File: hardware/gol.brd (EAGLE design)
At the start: 67.3 x 67.3 mm, 70 parts, among them J1 TC2050-IDC, J2 2057-MCR-B-S-RA-TSMT-NP-CS4-T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, U1 STM32F072CBT, U2 AP2111H-3.3TRG1SOT-223_DIO-M

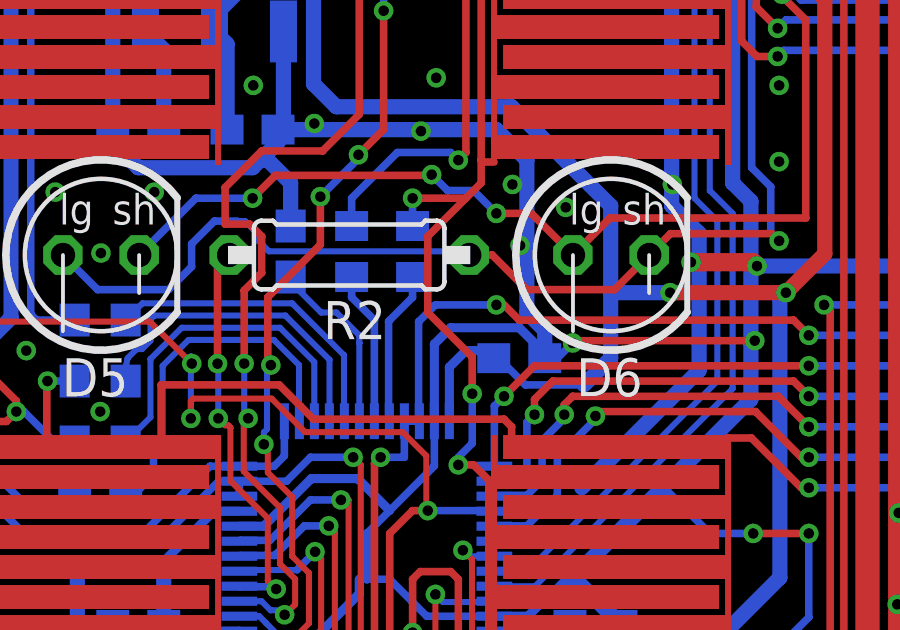
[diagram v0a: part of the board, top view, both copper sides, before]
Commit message: fills in an orphan
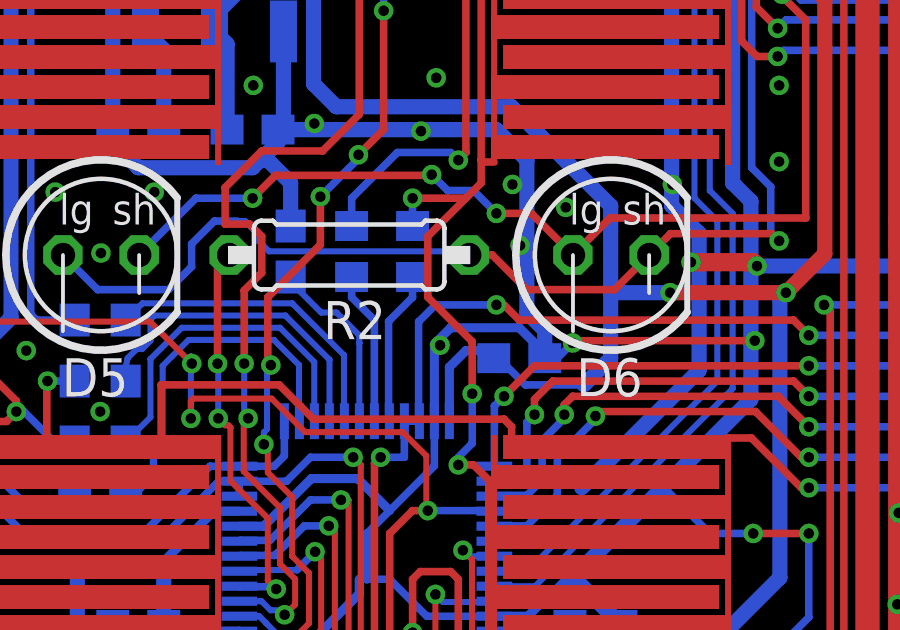
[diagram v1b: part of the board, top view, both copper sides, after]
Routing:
- net GND: vias 164 -> 165
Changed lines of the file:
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@@
 <via x="20.3708" y="11.0998" extent="1-16" drill="0.35"/>
 <via x="23.749" y="9.8806" extent="1-16" drill="0.35"/>
+<via x="24.0284" y="35.9918" extent="1-16" drill="0.35"/>
 </signal>
 <signal name="CAN_TR">
@@
 <wire x1="25.100803125" y1="32.720803125" x2="25.100803125" y2="34.377003125" width="0.254" layer="16"/>
 <via x="25.100803125" y="34.377003125" extent="1-16" drill="0.35"/>
-<wire x1="25.100803125" y1="34.377003125" x2="25.100803125" y2="35.605196875" width="0.254" layer="1"/>
-<wire x1="23.622" y1="37.084" x2="23.622" y2="39.624" width="0.254" layer="1"/>
+<wire x1="25.100803125" y1="34.377003125" x2="25.100803125" y2="36.113196875" width="0.254" layer="1"/>
+<wire x1="23.622" y1="37.592" x2="23.622" y2="39.624" width="0.254" layer="1"/>
 <wire x1="23.622" y1="39.624" x2="24.892" y2="40.894" width="0.254" layer="1"/>
 <wire x1="24.638" y1="32.258" x2="25.100803125" y2="32.720803125" width="0.254" layer="16"/>
-<wire x1="25.100803125" y1="35.605196875" x2="23.622" y2="37.084" width="0.254" layer="1"/>
+<wire x1="25.100803125" y1="36.113196875" x2="23.622" y2="37.592" width="0.254" layer="1"/>
 <wire x1="25.83" y1="25.1" x2="26.416" y2="24.514" width="0.254" layer="1"/>
 <wire x1="26.416" y1="24.514" x2="26.416" y2="24.384" width="0.254" layer="1"/>

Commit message: adds right-angle female header. replaces north with this.
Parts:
- BTN17: value BOOT -> FLASH
- NORTH: device pinhead:1X04/90 -> parts:JP4-RA-FEM
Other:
- board text added: "(c) bracz 2023-06-23"
- board text added: "+5V"
- board text added: "G"
- board text added: "GLB"
- board text added: "GND"
- board text added: "L"
- board text added: "LOC"
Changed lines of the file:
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@@
 <layers>
 <layer number="1" name="Top" color="4" fill="1" visible="yes" active="yes"/>
-<layer number="16" name="Bottom" color="1" fill="1" visible="yes" active="yes"/>
+<layer number="16" name="Bottom" color="1" fill="1" visible="no" active="yes"/>
 <layer number="17" name="Pads" color="2" fill="1" visible="yes" active="yes"/>
 <layer number="18" name="Vias" color="2" fill="1" visible="yes" active="yes"/>
@@
 <layer number="20" name="Dimension" color="24" fill="1" visible="yes" active="yes"/>
 <layer number="21" name="tPlace" color="7" fill="1" visible="yes" active="yes"/>
-<layer number="22" name="bPlace" color="7" fill="1" visible="yes" active="yes"/>
+<layer number="22" name="bPlace" color="7" fill="1" visible="no" active="yes"/>
 <layer number="23" name="tOrigins" color="15" fill="1" visible="yes" active="yes"/>
-<layer number="24" name="bOrigins" color="15" fill="1" visible="yes" active="yes"/>
+<layer number="24" name="bOrigins" color="15" fill="1" visible="no" active="yes"/>
 <layer number="25" name="tNames" color="7" fill="1" visible="yes" active="yes"/>
-<layer number="26" name="bNames" color="7" fill="1" visible="yes" active="yes"/>
+<layer number="26" name="bNames" color="7" fill="1" visible="no" active="yes"/>
 <layer number="27" name="tValues" color="7" fill="1" visible="no" active="yes"/>
 <layer number="28" name="bValues" color="7" fill="1" visible="no" active="yes"/>
@@
 <layer number="38" name="bTest" color="7" fill="1" visible="no" active="yes"/>
 <layer number="39" name="tKeepout" color="4" fill="11" visible="yes" active="yes"/>
-<layer number="40" name="bKeepout" color="1" fill="11" visible="yes" active="yes"/>
+<layer number="40" name="bKeepout" color="1" fill="11" visible="no" active="yes"/>
 <layer number="41" name="tRestrict" color="4" fill="10" visible="yes" active="yes"/>
-<layer number="42" name="bRestrict" color="1" fill="10" visible="yes" active="yes"/>
+<layer number="42" name="bRestrict" color="1" fill="10" visible="no" active="yes"/>
 <layer number="43" name="vRestrict" color="2" fill="10" visible="no" active="yes"/>
 <layer number="44" name="Drills" color="7" fill="1" visible="no" active="yes"/>
@@
 <layer number="50" name="dxf" color="7" fill="1" visible="no" active="no"/>
 <layer number="51" name="tDocu" color="7" fill="1" visible="yes" active="yes"/>
-<layer number="52" name="bDocu" color="7" fill="1" visible="yes" active="yes"/>
+<layer number="52" name="bDocu" color="7" fill="1" visible="no" active="yes"/>
 <layer number="53" name="tGND_GNDA" color="7" fill="9" visible="no" active="no"/>
 <layer number="54" name="bGND_GNDA" color="1" fill="9" visible="no" active="no"/>
@@
 <wire x1="2.54" y1="49.53" x2="0" y2="46.99" width="0" layer="20"/>
 <wire x1="0" y1="46.99" x2="0" y2="0" width="0" layer="20"/>
+<text x="3.81" y="33.782" size="1.27" layer="25">GND</text>
+<text x="59.436" y="33.782" size="1.27" layer="25">GND</text>
+<text x="42.164" y="7.874" size="1.27" layer="25" rot="R90">GND</text>
+<text x="41.148" y="52.578" size="1.27" layer="25" rot="R270">GND</text>
+<text x="34.036" y="52.578" size="1.27" layer="25" rot="R270">+5V</text>
+<text x="3.81" y="26.162" size="1.27" layer="25">+5V</text>
+<text x="35.306" y="7.874" size="1.27" layer="25" rot="R90">+5V</text>
+<text x="63.5" y="27.178" size="1.27" layer="25" rot="R180">+5V</text>
+<text x="38.862" y="52.578" size="1.27" layer="25" rot="R270">LOC</text>
+<text x="40.132" y="8.128" size="1.27" layer="25" rot="R90">LOC</text>
+<text x="5.334" y="31.242" size="1.27" layer="25">LOC</text>
+<text x="36.322" y="52.578" size="1.27" layer="25" rot="R270">GLB</text>
+<text x="37.592" y="7.874" size="1.27" layer="25" rot="R90">GLB</text>
+<text x="5.334" y="28.702" size="1.27" layer="25">GLB</text>
+<text x="62.23" y="29.718" size="1.27" layer="25" rot="R180">G</text>
+<text x="61.976" y="32.258" size="1.27" layer="25" rot="R180">L</text>
+<text x="3.556" y="59.69" size="1.27" layer="25" rot="R270">(c) bracz
+2023-06-23</text>
+<rectangle x1="34.544" y1="13.462" x2="41.91" y2="46.482" layer="25"/>
 </plain>
 <attributes>
@@
 <element name="BTN15" library="parts" package="COMB" value="BUTTON-CAP" x="46.73" y="12" smashed="yes"/>
 <element name="BTN16" library="parts" package="COMB" value="BUTTON-CAP" x="61.73" y="12" smashed="yes"/>
-<element name="BTN17" library="parts" package="COMB_EXPOSED" value="BOOT" x="4.064" y="20.574" smashed="yes">
+<element name="BTN17" library="parts" package="COMB_EXPOSED" value="FLASH" x="4.064" y="20.574" smashed="yes">
 <attribute name="VALUE" x="0.762" y="15.24" size="1.27" layer="21"/>
 </element>
@@
 <attribute name="VALUE" x="35.185" y="6.515" size="1.27" layer="27"/>
 </element>
-<element name="NORTH" library="pinhead" library_urn="urn:adsk.eagle:library:325" package="1X04/90" package3d_urn="urn:adsk.eagle:package:22404/2" value="NORTH" x="38.23" y="59.892" smashed="yes">
+<element name="NORTH" library="parts" package="JP4-RA-FEM" value="NORTH" x="38.23" y="59.892" smashed="yes">
 <attribute name="NAME" x="41.073" y="54.105" size="1.27" layer="25" ratio="10" rot="R180"/>
-<attribute name="POPULARITY" value="9" x="134.75" y="17.982" size="1.778" layer="27" display="off"/>
 <attribute name="VALUE" x="35.155" y="52.877" size="1.27" layer="27"/>
 </element>
@@
 </drawing>
 <compatibility>
+<note version="6.3" minversion="6.2.2" severity="warning">
+Since Version 6.2.2 text objects can contain more than one line,
+which will not be processed correctly with this version.
+</note>
 <note version="8.2" severity="warning">
 Since Version 8.2, EAGLE supports online libraries. The ids

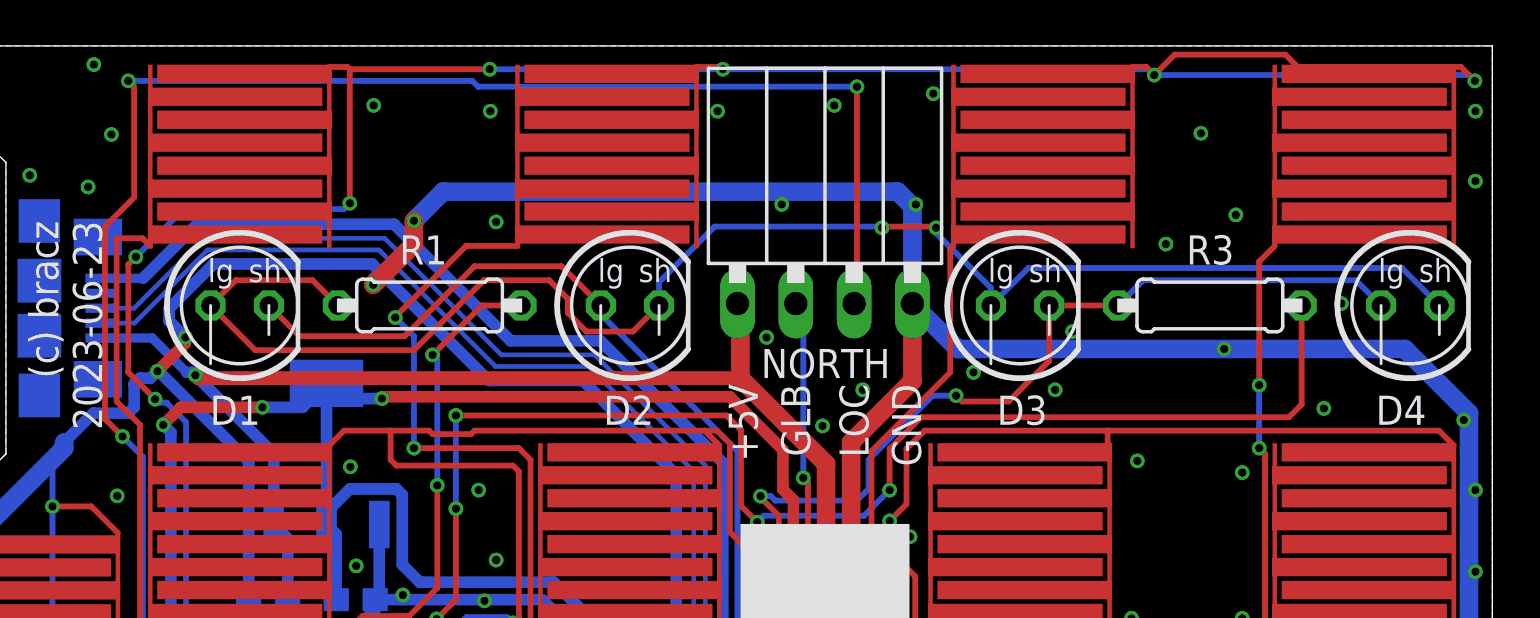
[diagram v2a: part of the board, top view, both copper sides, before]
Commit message: Realigns the north connector with the edge. Updates some ground vias.
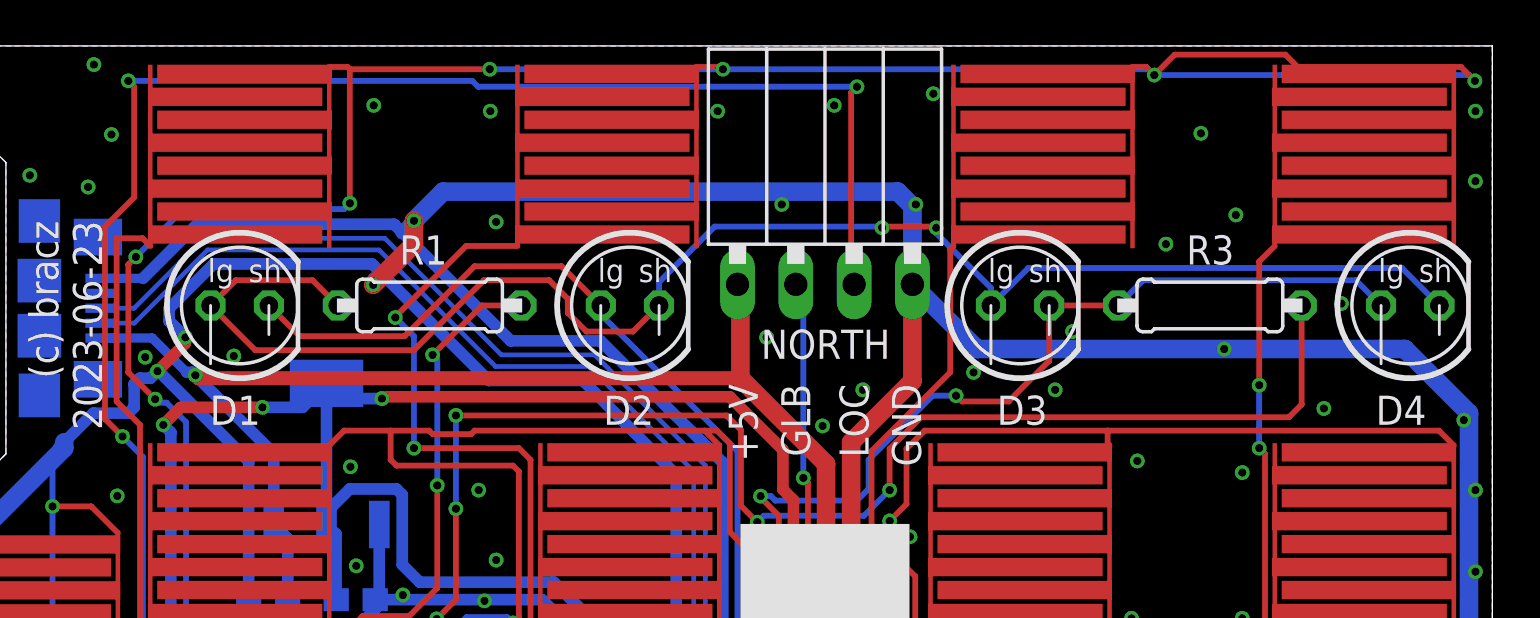
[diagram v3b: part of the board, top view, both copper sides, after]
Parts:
- moved NORTH 0.84 mm to (38.2, 60.7)
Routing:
- net GND: track 471.5 -> 472.5 mm, vias 165 -> 167
- net CAN_TR: track 206.0 -> 206.8 mm
- net +5V: track 213.0 -> 213.8 mm
- net NORTH: track 91.9 -> 91.2 mm
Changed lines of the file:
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@@
 <layers>
 <layer number="1" name="Top" color="4" fill="1" visible="yes" active="yes"/>
-<layer number="16" name="Bottom" color="1" fill="1" visible="no" active="yes"/>
+<layer number="16" name="Bottom" color="1" fill="1" visible="yes" active="yes"/>
 <layer number="17" name="Pads" color="2" fill="1" visible="yes" active="yes"/>
 <layer number="18" name="Vias" color="2" fill="1" visible="yes" active="yes"/>
 <layer number="19" name="Unrouted" color="6" fill="1" visible="yes" active="yes"/>
 <layer number="20" name="Dimension" color="24" fill="1" visible="yes" active="yes"/>
-<layer number="21" name="tPlace" color="7" fill="1" visible="yes" active="yes"/>
-<layer number="22" name="bPlace" color="7" fill="1" visible="no" active="yes"/>
-<layer number="23" name="tOrigins" color="15" fill="1" visible="yes" active="yes"/>
-<layer number="24" name="bOrigins" color="15" fill="1" visible="no" active="yes"/>
-<layer number="25" name="tNames" color="7" fill="1" visible="yes" active="yes"/>
-<layer number="26" name="bNames" color="7" fill="1" visible="no" active="yes"/>
+<layer number="21" name="tPlace" color="7" fill="1" visible="no" active="yes"/>
+<layer number="22" name="bPlace" color="7" fill="1" visible="yes" active="yes"/>
+<layer number="23" name="tOrigins" color="15" fill="1" visible="no" active="yes"/>
+<layer number="24" name="bOrigins" color="15" fill="1" visible="yes" active="yes"/>
+<layer number="25" name="tNames" color="7" fill="1" visible="no" active="yes"/>
+<layer number="26" name="bNames" color="7" fill="1" visible="yes" active="yes"/>
 <layer number="27" name="tValues" color="7" fill="1" visible="no" active="yes"/>
 <layer number="28" name="bValues" color="7" fill="1" visible="no" active="yes"/>
@@
 <layer number="37" name="tTest" color="7" fill="1" visible="no" active="yes"/>
 <layer number="38" name="bTest" color="7" fill="1" visible="no" active="yes"/>
-<layer number="39" name="tKeepout" color="4" fill="11" visible="yes" active="yes"/>
-<layer number="40" name="bKeepout" color="1" fill="11" visible="no" active="yes"/>
-<layer number="41" name="tRestrict" color="4" fill="10" visible="yes" active="yes"/>
-<layer number="42" name="bRestrict" color="1" fill="10" visible="no" active="yes"/>
+<layer number="39" name="tKeepout" color="4" fill="11" visible="no" active="yes"/>
+<layer number="40" name="bKeepout" color="1" fill="11" visible="yes" active="yes"/>
+<layer number="41" name="tRestrict" color="4" fill="10" visible="no" active="yes"/>
+<layer number="42" name="bRestrict" color="1" fill="10" visible="yes" active="yes"/>
 <layer number="43" name="vRestrict" color="2" fill="10" visible="no" active="yes"/>
 <layer number="44" name="Drills" color="7" fill="1" visible="no" active="yes"/>
@@
 <layer number="49" name="Reference" color="7" fill="1" visible="no" active="yes"/>
 <layer number="50" name="dxf" color="7" fill="1" visible="no" active="no"/>
-<layer number="51" name="tDocu" color="7" fill="1" visible="yes" active="yes"/>
-<layer number="52" name="bDocu" color="7" fill="1" visible="no" active="yes"/>
+<layer number="51" name="tDocu" color="7" fill="1" visible="no" active="yes"/>
+<layer number="52" name="bDocu" color="7" fill="1" visible="yes" active="yes"/>
 <layer number="53" name="tGND_GNDA" color="7" fill="9" visible="no" active="no"/>
 <layer number="54" name="bGND_GNDA" color="1" fill="9" visible="no" active="no"/>
@@
 <attribute name="VALUE" x="35.185" y="6.515" size="1.27" layer="27"/>
 </element>
-<element name="NORTH" library="parts" package="JP4-RA-FEM" value="NORTH" x="38.23" y="59.892" smashed="yes">
-<attribute name="NAME" x="41.073" y="54.105" size="1.27" layer="25" ratio="10" rot="R180"/>
-<attribute name="VALUE" x="35.155" y="52.877" size="1.27" layer="27"/>
+<element name="NORTH" library="parts" package="JP4-RA-FEM" value="NORTH" x="38.23" y="60.7302" smashed="yes">
+<attribute name="NAME" x="41.073" y="54.9432" size="1.27" layer="25" ratio="10" rot="R180"/>
+<attribute name="VALUE" x="35.155" y="53.7152" size="1.27" layer="27"/>
 </element>
 <element name="EAST" library="parts" package="1X04" value="EAST" x="66.04" y="30.48" smashed="yes" rot="R90">
@@
 <wire x1="23.84" y1="31.968" x2="22.352" y2="30.48" width="0.254" layer="16"/>
 <wire x1="22.352" y1="30.48" x2="21.59" y2="29.718" width="0.254" layer="16"/>
-<wire x1="42.04" y1="56.082" x2="42.04" y2="52.708" width="0.8128" layer="1"/>
+<wire x1="42.04" y1="56.9202" x2="42.04" y2="52.708" width="0.8128" layer="1"/>
 <wire x1="42.04" y1="6.982" x2="42.04" y2="4.51" width="0.8128" layer="1"/>
 <wire x1="42.04" y1="52.708" x2="39.37" y2="50.038" width="0.8128" layer="1"/>
@@
 <wire x1="8.5136" y1="57.18" x2="10.8712" y2="59.5376" width="0.508" layer="16"/>
 <wire x1="10.8712" y1="59.5376" x2="19.4564" y2="59.5376" width="0.508" layer="16"/>
-<wire x1="19.4564" y1="59.5376" x2="24.5364" y2="54.4576" width="0.508" layer="16"/>
+<wire x1="19.4564" y1="59.5376" x2="19.812" y2="59.182" width="0.508" layer="16"/>
+<wire x1="19.812" y1="59.182" x2="24.5364" y2="54.4576" width="0.508" layer="16"/>
 <wire x1="24.5364" y1="54.4576" x2="28.448" y2="54.4576" width="0.508" layer="16"/>
 <wire x1="28.448" y1="54.4576" x2="33.782" y2="49.149" width="0.508" layer="16"/>
@@
 <via x="32.3942" y="38.7604" extent="1-16" drill="0.35"/>
 <wire x1="32.3942" y1="38.7604" x2="32.6644" y2="38.7604" width="0.3048" layer="16"/>
-<wire x1="42.04" y1="56.082" x2="44.02" y2="54.102" width="0.8128" layer="16"/>
+<wire x1="42.04" y1="56.9202" x2="44.8582" y2="54.102" width="0.8128" layer="16"/>
 <wire x1="66.294" y1="34.544" x2="66.04" y2="34.29" width="0.8128" layer="16"/>
-<wire x1="44.02" y1="54.102" x2="63.5" y2="54.102" width="0.8128" layer="16"/>
+<wire x1="44.8582" y1="54.102" x2="63.5" y2="54.102" width="0.8128" layer="16"/>
 <wire x1="63.5" y1="54.102" x2="66.294" y2="51.308" width="0.8128" layer="16"/>
 <wire x1="66.294" y1="51.308" x2="66.294" y2="34.544" width="0.8128" layer="16"/>
@@
 <wire x1="20.32" y1="58.674" x2="20.32" y2="59.69" width="0.8128" layer="1"/>
 <wire x1="41.402" y1="60.96" x2="42.04" y2="60.322" width="0.8128" layer="16"/>
-<wire x1="42.04" y1="60.322" x2="42.04" y2="56.082" width="0.8128" layer="16"/>
+<wire x1="42.04" y1="60.322" x2="42.04" y2="56.9202" width="0.8128" layer="16"/>
 <polygon width="0.1524" layer="1" spacing="0.508" pour="hatch" isolate="0.254">
 <vertex x="0" y="67.31"/>
@@
 <via x="23.749" y="9.8806" extent="1-16" drill="0.35"/>
 <via x="24.0284" y="35.9918" extent="1-16" drill="0.35"/>
+<wire x1="19.812" y1="59.182" x2="20.32" y2="59.69" width="0.6096" layer="16"/>
+<via x="8.6106" y="53.7464" extent="1-16" drill="0.35"/>
+<via x="12.4714" y="53.7972" extent="1-16" drill="0.35"/>
 </signal>
 <signal name="CAN_TR">
@@
 <wire x1="37.4904" y1="48.2854" x2="37.2872" y2="48.4886" width="0.254" layer="1"/>
 <via x="37.2872" y="48.4886" extent="1-16" drill="0.35"/>
-<wire x1="37.2872" y1="48.4886" x2="37.2872" y2="55.7548" width="0.254" layer="16"/>
-<wire x1="37.2872" y1="55.7548" x2="36.96" y2="56.082" width="0.254" layer="16"/>
+<wire x1="37.2872" y1="48.4886" x2="37.2872" y2="56.593" width="0.254" layer="16"/>
+<wire x1="37.2872" y1="56.593" x2="36.96" y2="56.9202" width="0.254" layer="16"/>
 <wire x1="37.4904" y1="11.8364" x2="37.4904" y2="23.0886" width="0.254" layer="1"/>
 <wire x1="37.4904" y1="23.0886" x2="37.4904" y2="48.2854" width="0.254" layer="1"/>
@@
 <wire x1="23.114" y1="65.532" x2="39.624" y2="65.532" width="0.254" layer="16"/>
 <via x="39.624" y="65.532" extent="1-16" drill="0.35"/>
-<wire x1="39.624" y1="65.532" x2="39.624" y2="56.206" width="0.254" layer="1"/>
-<wire x1="39.624" y1="56.206" x2="39.5" y2="56.082" width="0.254" layer="1"/>
+<wire x1="39.5" y1="56.9202" x2="39.37" y2="57.0502" width="0.254" layer="1"/>
+<wire x1="39.624" y1="65.532" x2="39.37" y2="65.278" width="0.254" layer="1"/>
+<wire x1="39.37" y1="65.278" x2="39.37" y2="57.0502" width="0.254" layer="1"/>
 <wire x1="10.033" y1="29.845" x2="7.62" y2="32.258" width="0.254" layer="16"/>
 <wire x1="6.858" y1="32.512" x2="6.858" y2="35.052" width="0.254" layer="16"/>
@@
 <wire x1="14.21" y1="46.4542" x2="14.82" y2="45.8442" width="0.508" layer="16"/>
 <wire x1="14.82" y1="45.8442" x2="14.82" y2="43.18" width="0.508" layer="16"/>
-<wire x1="34.42" y1="56.082" x2="34.544" y2="55.958" width="0.8128" layer="1"/>
+<wire x1="34.42" y1="56.9202" x2="34.544" y2="56.7962" width="0.8128" layer="1"/>
 <wire x1="34.42" y1="6.5308" x2="34.42" y2="4.51" width="0.8128" layer="1"/>
-<wire x1="34.544" y1="55.958" x2="34.544" y2="52.832" width="0.8128" layer="1"/>
+<wire x1="34.544" y1="56.7962" x2="34.544" y2="52.832" width="0.8128" layer="1"/>
 <wire x1="34.544" y1="52.832" x2="38.2778" y2="49.0982" width="0.8128" layer="1"/>
 <wire x1="38.2778" y1="49.0982" x2="38.2778" y2="10.3886" width="0.8128" layer="1"/>
